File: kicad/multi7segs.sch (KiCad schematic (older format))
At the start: 9 parts

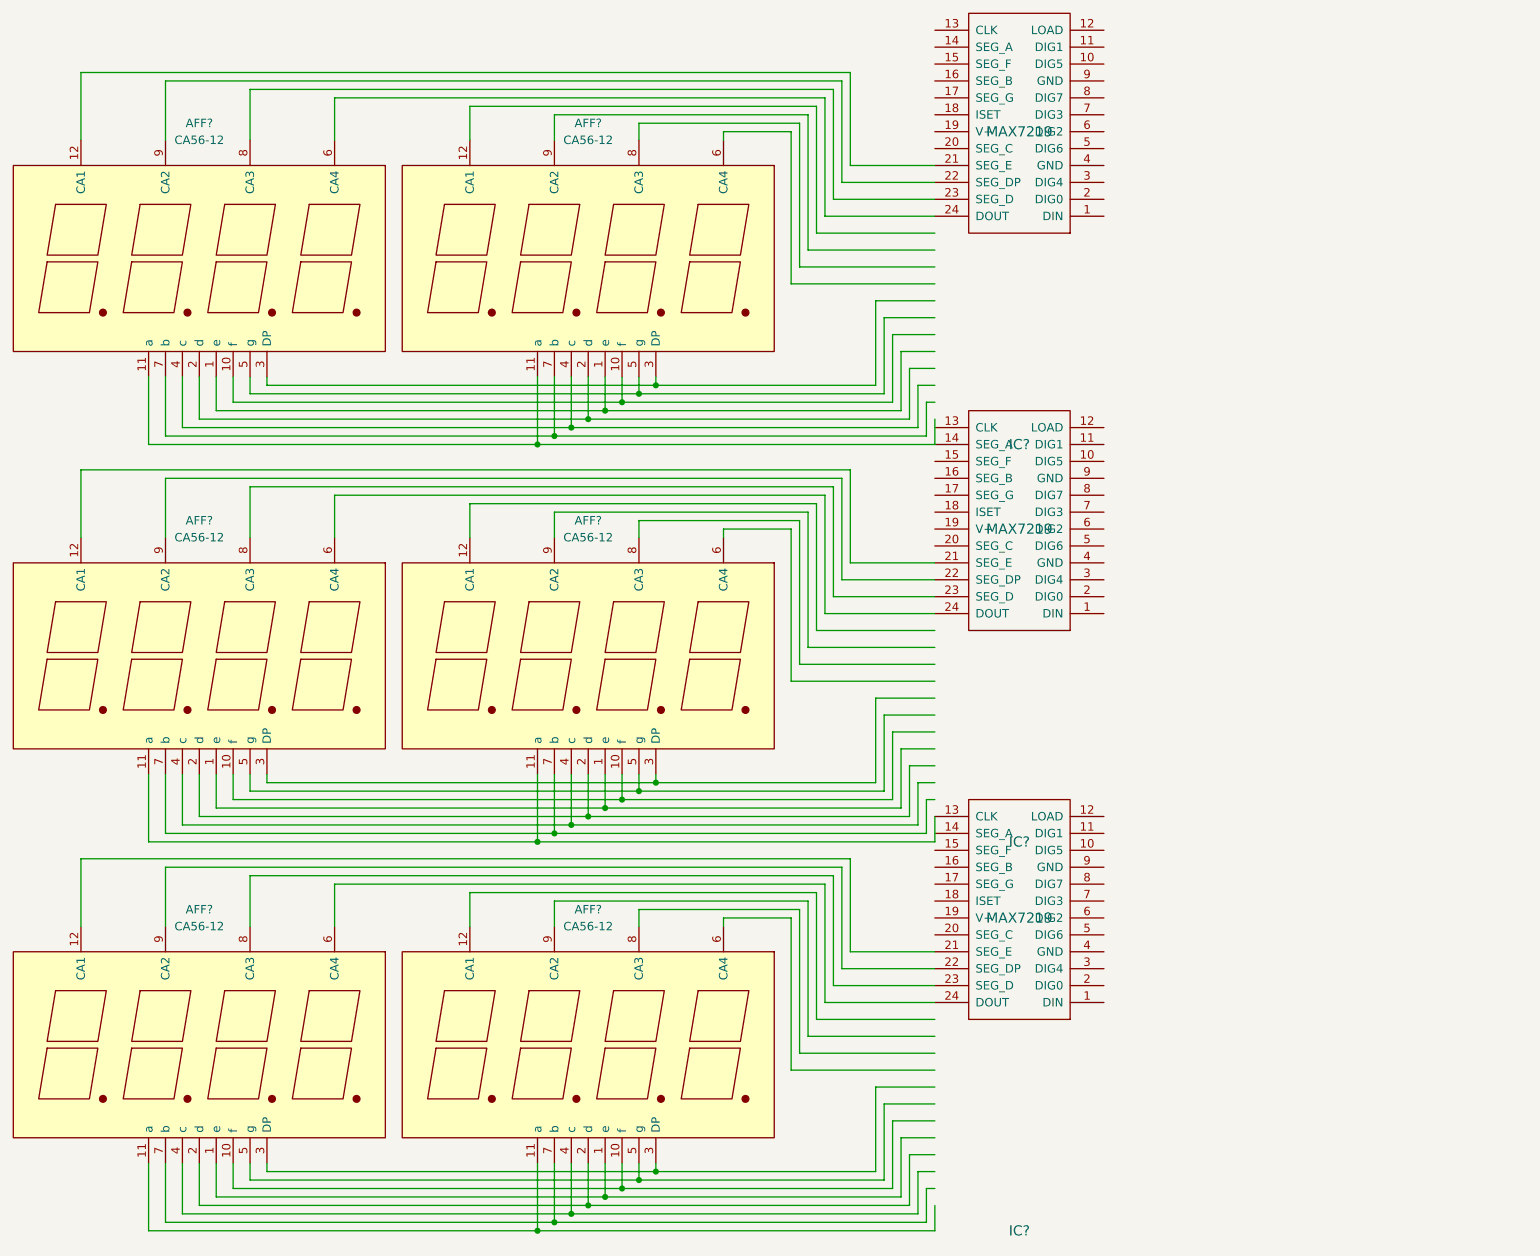
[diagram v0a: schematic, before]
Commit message: Common anode displays
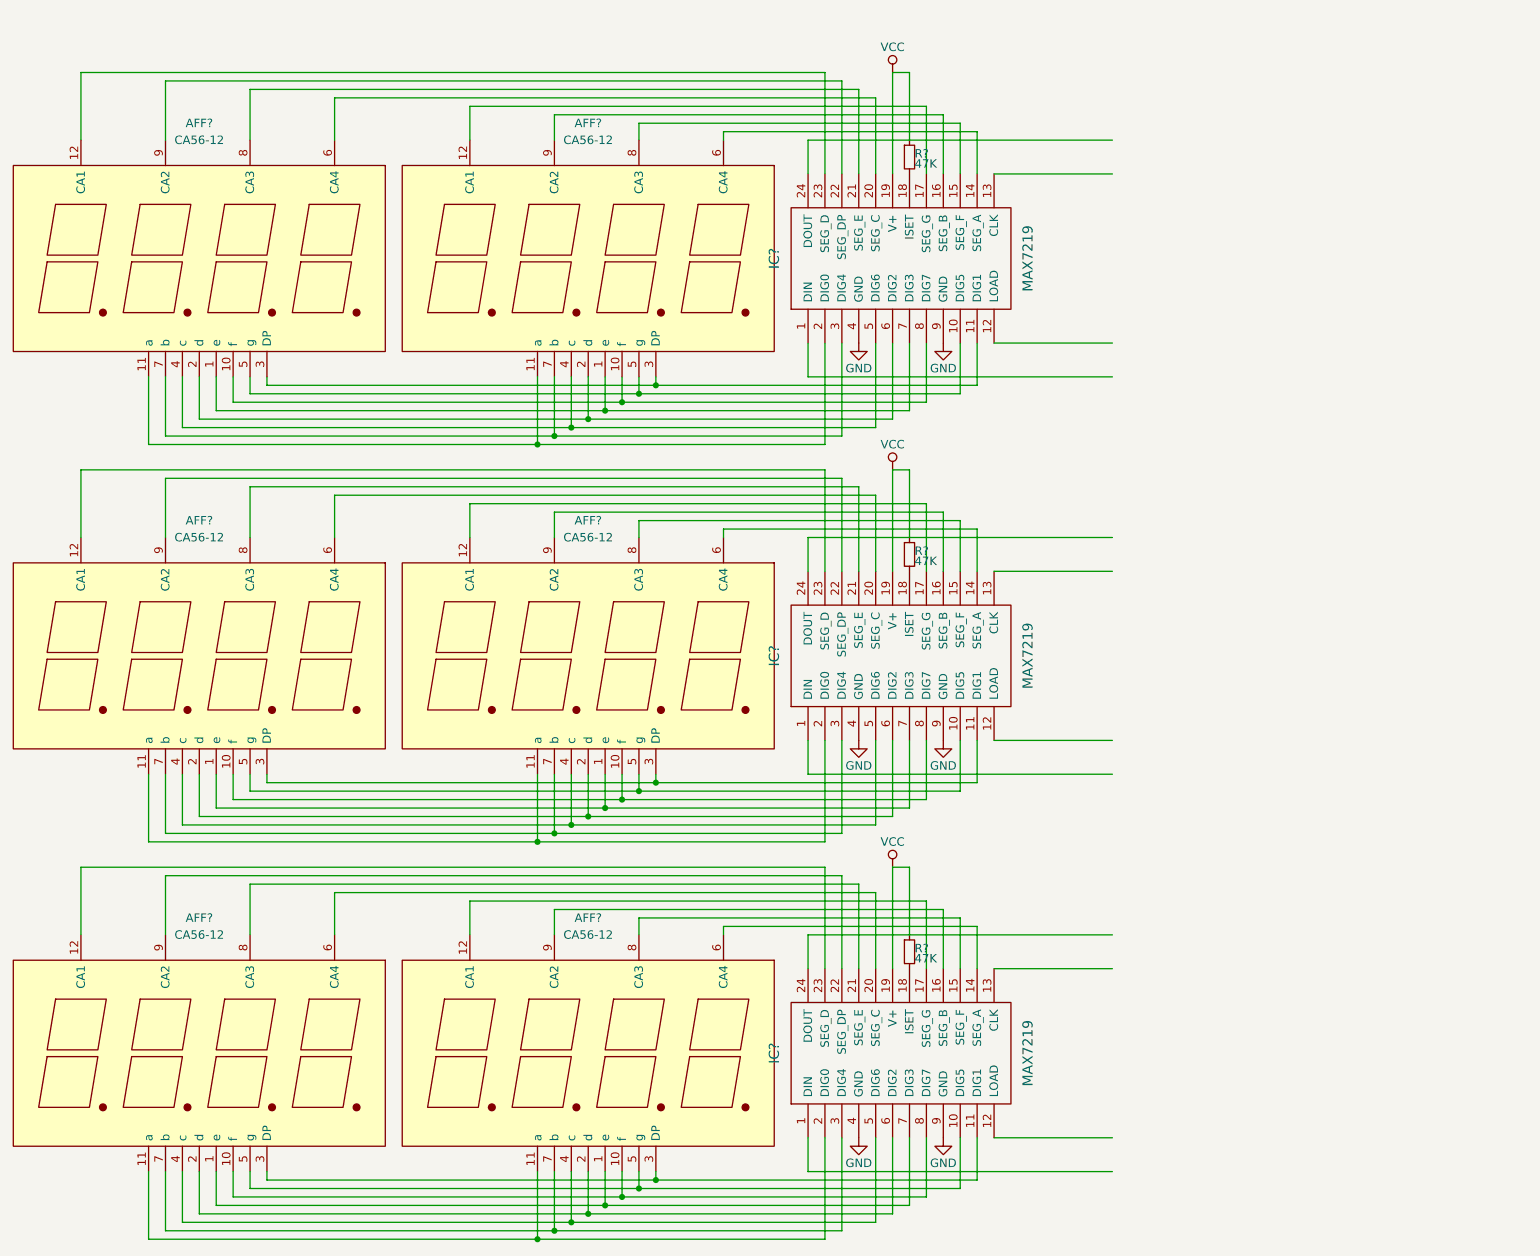
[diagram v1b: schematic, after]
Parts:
- removed AFF? (x4): CA56-12, symbol CA56-12
- removed IC? (x3): MAX7219, symbol MAX7219
- added AFF? (x4): CA56-12, symbol CA56-12
- added IC? (x3): MAX7219, symbol MAX7219
- added R? (x3): 47K, symbol R_Small
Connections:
- net labels added: GND, VCC
- wire segments 237 -> 219

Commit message: "Realistic" wiring
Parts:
- removed AFF? (x6): CA56-12, symbol CA56-12
- removed IC? (x2): MAX7219, symbol MAX7219
- removed R? (x2): 47K, symbol R_Small
- added AFF? (x2): 7segsCAx4, symbol 7segsCAx4
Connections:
- wire segments 219 -> 60
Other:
- moved on the sheet: IC?, R?

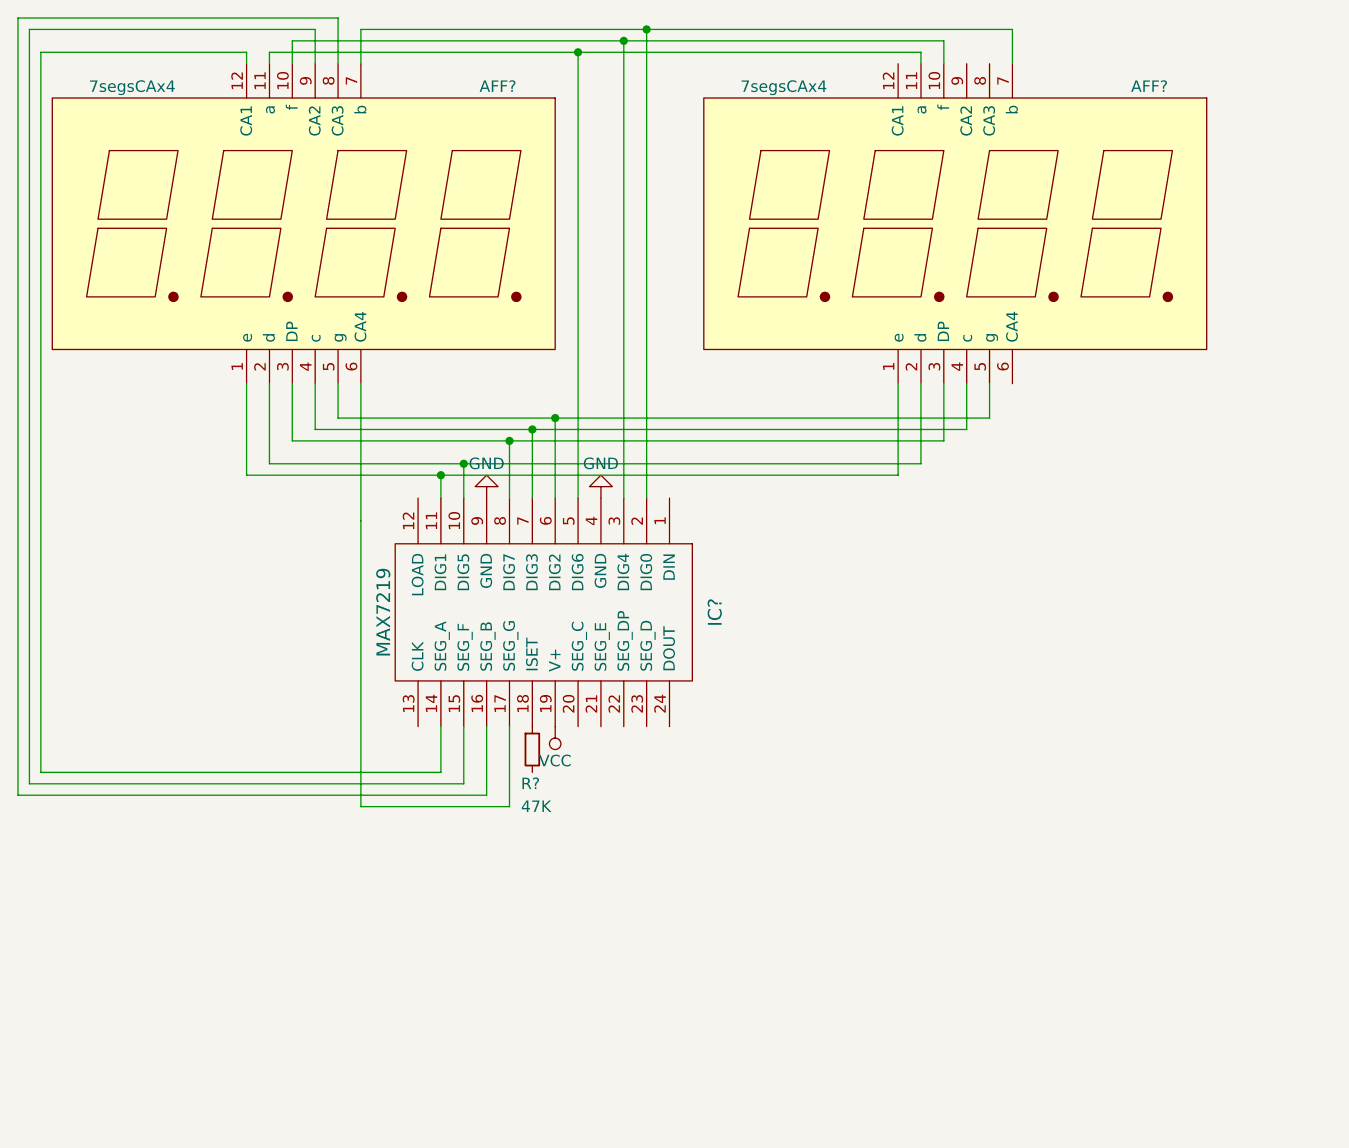
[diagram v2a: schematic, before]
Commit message: Use labels on the schematic
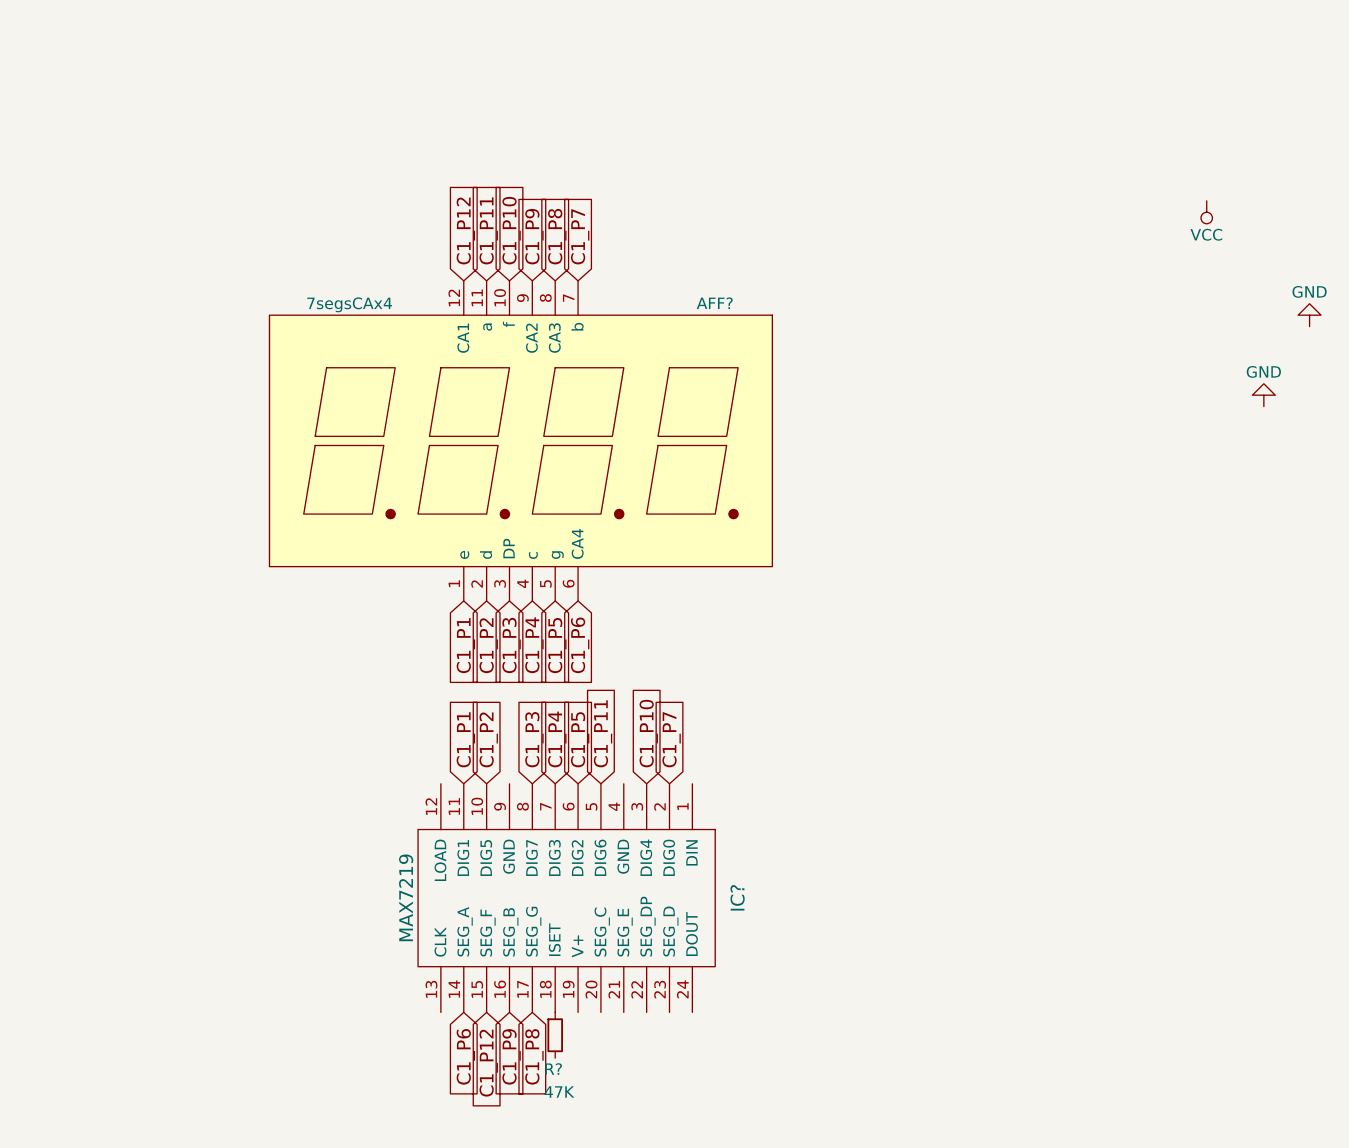
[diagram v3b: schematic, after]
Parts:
- removed AFF?: 7segsCAx4, symbol 7segsCAx4
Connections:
- net GND: no longer IC?.4 (GND), IC?.9 (GND)
- net VCC: no longer IC?.19 (V+)
- net C1_P2: now reaches AFF?.2 (d), IC?.10 (DIG5)
- net C1_P1: now reaches AFF?.1 (e), IC?.11 (DIG1)
- net C1_P6: now reaches IC?.14 (SEG_A)
- net C1_P6: now also AFF?.6 (CA4)
- net C1_P12: now reaches IC?.15 (SEG_F)
- net C1_P12: now also AFF?.12 (CA1)
- net C1_P9: now reaches IC?.16 (SEG_B)
- net C1_P9: now also AFF?.9 (CA2)
- net C1_P8: now reaches IC?.17 (SEG_G)
- net C1_P8: now also AFF?.8 (CA3)
- net C1_P7: now reaches AFF?.7 (b), IC?.2 (DIG0)
- net C1_P10: now reaches AFF?.10 (f), IC?.3 (DIG4)
- net C1_P11: now reaches AFF?.11 (a), IC?.5 (DIG6)
- net C1_P5: now reaches AFF?.5 (g), IC?.6 (DIG2)
- net C1_P4: now reaches AFF?.4 (c), IC?.7 (DIG3)
- net C1_P3: now reaches AFF?.3 (DP), IC?.8 (DIG7)
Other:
- moved on the sheet: AFF?, IC?, R?

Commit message: Not all labels
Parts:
- added AFF? (x5): 7segsCAx4, symbol 7segsCAx4
- added IC? (x2): MAX7219, symbol MAX7219
- added R? (x2): 47K, symbol R_Small
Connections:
- net C1_P1: now also AFF?.1 (e), AFF?.1 (e), AFF?.1 (e), AFF?.1 (e), AFF?.1 (e), IC?.11 (DIG1), IC?.11 (DIG1)
- net C1_P10: now also AFF?.10 (f), AFF?.10 (f), AFF?.10 (f), AFF?.10 (f), AFF?.10 (f), IC?.3 (DIG4), IC?.3 (DIG4)
- net C1_P11: now also AFF?.11 (a), AFF?.11 (a), AFF?.11 (a), AFF?.11 (a), AFF?.11 (a), IC?.5 (DIG6), IC?.5 (DIG6)
- net C1_P2: now also AFF?.2 (d), AFF?.2 (d), AFF?.2 (d), AFF?.2 (d), AFF?.2 (d), IC?.10 (DIG5), IC?.10 (DIG5)
- net C1_P3: now also AFF?.3 (DP), AFF?.3 (DP), AFF?.3 (DP), AFF?.3 (DP), AFF?.3 (DP), IC?.8 (DIG7), IC?.8 (DIG7)
- net C1_P4: now also AFF?.4 (c), AFF?.4 (c), AFF?.4 (c), AFF?.4 (c), AFF?.4 (c), IC?.7 (DIG3), IC?.7 (DIG3)
- net C1_P5: now also AFF?.5 (g), AFF?.5 (g), AFF?.5 (g), AFF?.5 (g), AFF?.5 (g), IC?.6 (DIG2), IC?.6 (DIG2)
- net C1_P7: now also AFF?.7 (b), AFF?.7 (b), AFF?.7 (b), AFF?.7 (b), AFF?.7 (b), IC?.2 (DIG0), IC?.2 (DIG0)
- net GND: now also IC?.4 (GND), IC?.9 (GND), IC?.4 (GND), IC?.4 (GND), IC?.9 (GND), IC?.9 (GND)
- net VCC: now also IC?.19 (V+), R?.2, IC?.19 (V+), IC?.19 (V+), R?.2, R?.2
- net at IC?.20 (SEG_C): now also AFF?.6 (CA4)
- net at IC?.21 (SEG_E): now also AFF?.12 (CA1)
- net at IC?.22 (SEG_DP): now also AFF?.9 (CA2)
- net at IC?.23 (SEG_D): now also AFF?.8 (CA3)
- net C1_P12: no longer names the net of AFF?.12 (CA1), IC?.15 (SEG_F)
- net C1_P6: no longer names the net of AFF?.6 (CA4), IC?.14 (SEG_A)
- net C1_P8: no longer names the net of AFF?.8 (CA3), IC?.17 (SEG_G)
- net C1_P9: no longer names the net of AFF?.9 (CA2), IC?.16 (SEG_B)
- new net: AFF?.6 (CA4), IC?.14 (SEG_A) (x2)
- new net: AFF?.12 (CA1), IC?.15 (SEG_F) (x2)
- new net: AFF?.9 (CA2), IC?.16 (SEG_B) (x2)
- new net: AFF?.8 (CA3), IC?.17 (SEG_G) (x2)
- new net: IC?.18 (ISET), R?.1 (x2)
- new net: AFF?.6 (CA4), IC?.20 (SEG_C) (x2)
- new net: AFF?.12 (CA1), IC?.21 (SEG_E) (x2)
- new net: AFF?.9 (CA2), IC?.22 (SEG_DP) (x2)
- new net: AFF?.8 (CA3), IC?.23 (SEG_D) (x2)
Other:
- moved on the sheet: AFF?, IC?, R?
